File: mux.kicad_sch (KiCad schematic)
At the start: 6 parts, among them U24002 4066, U24003 4066, U24004 4075

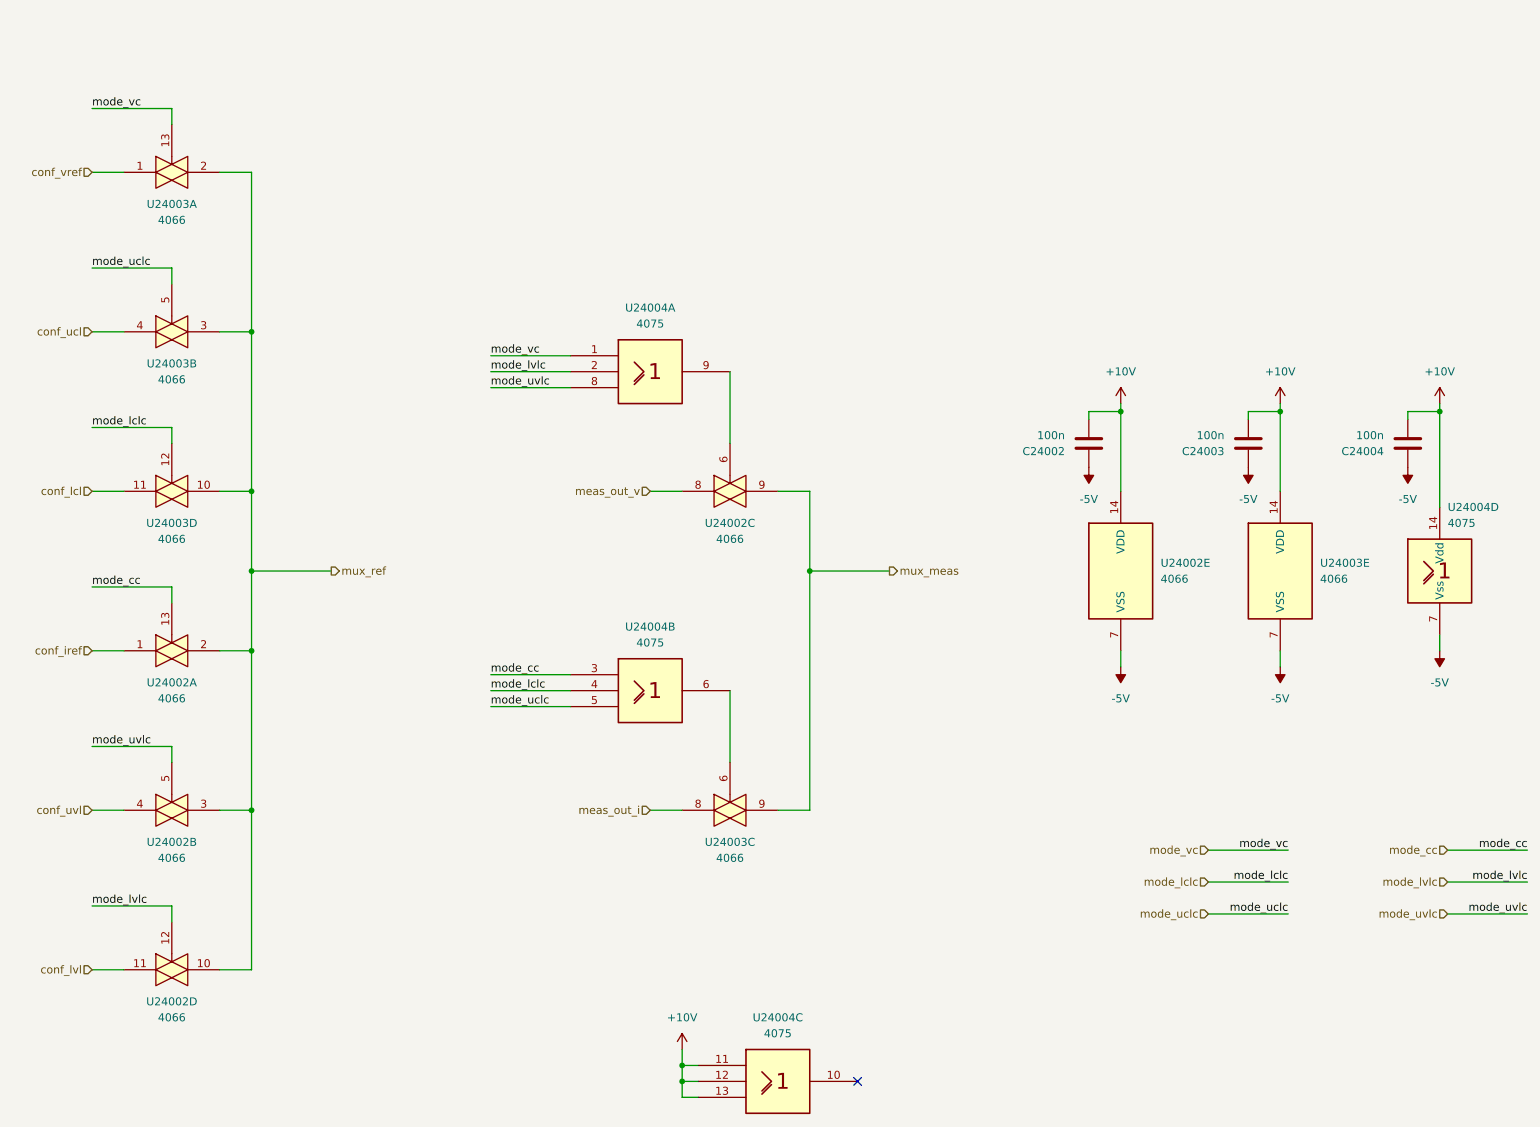
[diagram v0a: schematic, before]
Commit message: edit pss individual power nets for sub circuits
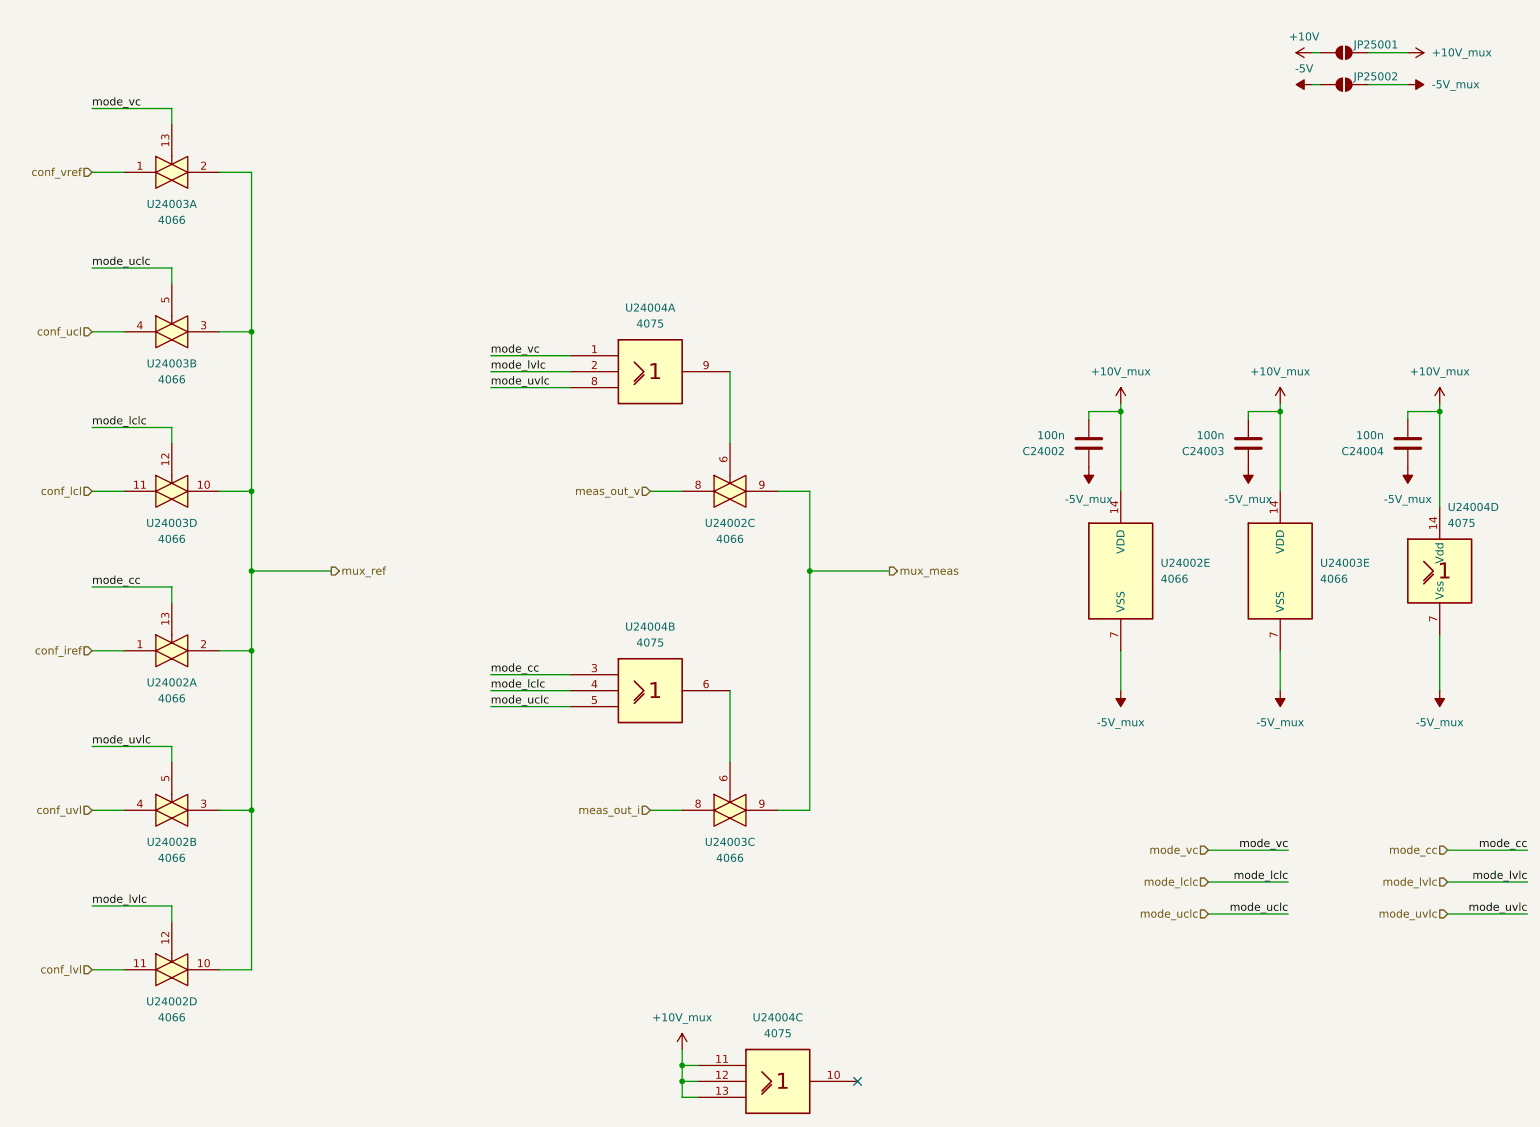
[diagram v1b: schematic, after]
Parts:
- added JP25001, JP25002: SolderJumper_2_Open, symbol Jumper:SolderJumper_2_Open
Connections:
- net +10V: now also JP25001.1 (A); no longer C24002.2, C24003.2, C24004.2, U24002.14 (VDD), U24003.14 (VDD), U24004.11, U24004.12, U24004.13, U24004.14 (Vdd)
- net -5V: now also JP25002.1 (A); no longer C24002.1, C24003.1, C24004.1, U24002.7 (VSS), U24003.7 (VSS), U24004.7 (Vss)
- new net +10V_mux: C24002.2, C24003.2, C24004.2, JP25001.2 (B), U24002.14 (VDD), U24003.14 (VDD), U24004.11, U24004.12, U24004.13, U24004.14 (Vdd)
- new net -5V_mux: C24002.1, C24003.1, C24004.1, JP25002.2 (B), U24002.7 (VSS), U24003.7 (VSS), U24004.7 (Vss)

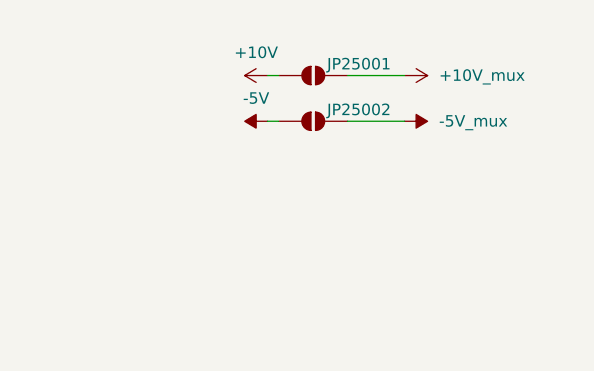
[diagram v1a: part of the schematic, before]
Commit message: fix pss ERC error: missing power flag
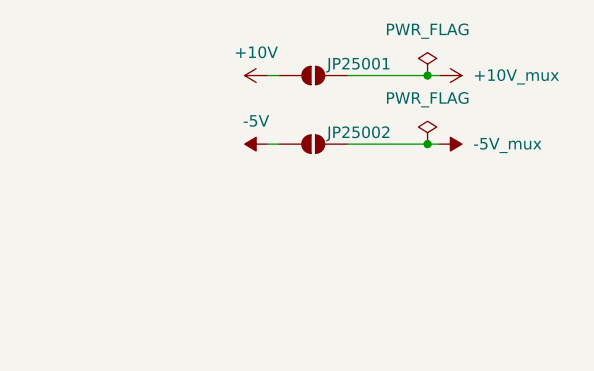
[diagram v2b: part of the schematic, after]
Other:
- moved on the sheet: JP25002
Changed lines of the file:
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@@
 	)
 	(junction
+		(at 262.89 25.4)
+		(diameter 0)
+		(color 0 0 0 0)
+	)
+	(junction
 		(at 240.03 82.55)
 		(diameter 0)
@@
 	)
 	(junction
+		(at 262.89 33.02)
+		(diameter 0)
+		(color 0 0 0 0)
+	)
+	(junction
 		(at 144.78 186.69)
 		(diameter 0)
@@
 	(wire
 		(pts
+			(xy 262.89 33.02) (xy 264.16 33.02)
+		)
+		(stroke
+			(width 0)
+			(type default)
+		)
+	)
+	(wire
+		(pts
 			(xy 234.95 83.82) (xy 234.95 82.55)
 		)
@@
 	(wire
 		(pts
-			(xy 245.11 30.48) (xy 246.38 30.48)
+			(xy 245.11 33.02) (xy 246.38 33.02)
 		)
 		(stroke
@@
 	(wire
 		(pts
-			(xy 254 30.48) (xy 260.35 30.48)
+			(xy 254 33.02) (xy 262.89 33.02)
 		)
 		(stroke
@@
 	(wire
 		(pts
-			(xy 254 25.4) (xy 260.35 25.4)
+			(xy 254 25.4) (xy 262.89 25.4)
 		)
 		(stroke
@@
 	(wire
 		(pts
+			(xy 262.89 25.4) (xy 264.16 25.4)
+		)
+		(stroke
+			(width 0)
+			(type default)
+		)
+	)
+	(wire
+		(pts
 			(xy 240.03 81.28) (xy 240.03 82.55)
 		)
@@
 	)
 	(symbol
+		(lib_id "pss:PWR_FLAG")
+		(at 262.89 33.02 0)
+		(unit 1)
+		(exclude_from_sim no)
+		(in_bom yes)
+		(on_board yes)
+		(dnp no)
+		(fields_autoplaced yes)
+		(property "Reference" "#FLG025002"
+			(at 262.89 31.115 0)
+			(effects
+				(font
+					(size 1.27 1.27)
+				)
+				(hide yes)
+			)
+		)
+		(property "Value" "PWR_FLAG"
+			(at 262.89 27.94 0)
+			(effects
+				(font
+					(size 1.27 1.27)
+				)
+			)
+		)
+		(property "Footprint" ""
+			(at 262.89 33.02 0)
+			(effects
+				(font
+					(size 1.27 1.27)
+				)
+				(hide yes)
+			)
+		)
+		(property "Datasheet" "~"
+			(at 262.89 33.02 0)
+			(effects
+				(font
+					(size 1.27 1.27)
+				)
+				(hide yes)
+			)
+		)
+		(property "Description" "Special symbol for telling ERC where power comes from"
+			(at 262.89 33.02 0)
+			(effects
+				(font
+					(size 1.27 1.27)
+				)
+				(hide yes)
+			)
+		)
+		(pin "1"
+		)
+		(instances
+			(project "pss"
+				(path "/3c438cf7-9350-4e9f-8115-1deba8984176/edd130f8-6d8c-4786-9c45-2e5306ef5419"
+					(reference "#FLG025002")
+					(unit 1)
+				)
+			)
+		)
+	)
+	(symbol
+		(lib_id "pss:PWR_FLAG")
+		(at 262.89 25.4 0)
+		(unit 1)
+		(exclude_from_sim no)
+		(in_bom yes)
+		(on_board yes)
+		(dnp no)
+		(fields_autoplaced yes)
+		(property "Reference" "#FLG025001"
+			(at 262.89 23.495 0)
+			(effects
+				(font
+					(size 1.27 1.27)
+				)
+				(hide yes)
+			)
+		)
+		(property "Value" "PWR_FLAG"
+			(at 262.89 20.32 0)
+			(effects
+				(font
+					(size 1.27 1.27)
+				)
+			)
+		)
+		(property "Footprint" ""
+			(at 262.89 25.4 0)
+			(effects
+				(font
+					(size 1.27 1.27)
+				)
+				(hide yes)
+			)
+		)
+		(property "Datasheet" "~"
+			(at 262.89 25.4 0)
+			(effects
+				(font
+					(size 1.27 1.27)
+				)
+				(hide yes)
+			)
+		)
+		(property "Description" "Special symbol for telling ERC where power comes from"
+			(at 262.89 25.4 0)
+			(effects
+				(font
+					(size 1.27 1.27)
+				)
+				(hide yes)
+			)
+		)
+		(pin "1"
+		)
+		(instances
+			(project "pss"
+				(path "/3c438cf7-9350-4e9f-8115-1deba8984176/edd130f8-6d8c-4786-9c45-2e5306ef5419"
+					(reference "#FLG025001")
+					(unit 1)
+				)
+			)
+		)
+	)
+	(symbol
 		(lib_id "pss:4075")
 		(at 160.02 189.23 0)
@@
 	(symbol
 		(lib_id "Jumper:SolderJumper_2_Open")
-		(at 250.19 30.48 0)
+		(at 250.19 33.02 0)
 		(unit 1)
 		(exclude_from_sim yes)
@@
 		(dnp no)
 		(property "Reference" "JP25002"
-			(at 255.27 29.21 0)
+			(at 255.27 31.75 0)
 			(effects
 				(font
@@
 		)
 		(property "Value" "SolderJumper_2_Open"
-			(at 224.79 17.78 0)
+			(at 224.79 20.32 0)
 			(effects
 				(font
@@
 		)
 		(property "Footprint" ""
-			(at 250.19 30.48 0)
+			(at 250.19 33.02 0)
 			(effects
 				(font
@@
 		)
 		(property "Datasheet" "~"
-			(at 250.19 30.48 0)
+			(at 250.19 33.02 0)
 			(effects
 				(font
@@
 		)
 		(property "Description" "Solder Jumper, 2-pole, open"
-			(at 250.19 30.48 0)
+			(at 250.19 33.02 0)
 			(effects
 				(font
@@
 	(symbol
 		(lib_id "pss:-5V_mux")
-		(at 260.35 30.48 270)
+		(at 264.16 33.02 270)
 		(unit 1)
 		(exclude_from_sim no)
@@
 		(fields_autoplaced yes)
 		(property "Reference" "#PWR025012"
-			(at 256.54 30.48 0)
+			(at 260.35 33.02 0)
 			(effects
 				(font
@@
 		)
 		(property "Value" "-5V_mux"
-			(at 264.16 30.4799 90)
+			(at 267.97 33.0199 90)
 			(effects
 				(font
@@
 		)
 		(property "Footprint" ""
-			(at 260.35 30.48 0)
+			(at 264.16 33.02 0)
 			(effects
 				(font
@@
 		)
 		(property "Datasheet" ""
-			(at 260.35 30.48 0)
+			(at 264.16 33.02 0)
 			(effects
 				(font
@@
 		)
 		(property "Description" ""
-			(at 260.35 30.48 0)
+			(at 264.16 33.02 0)
 			(effects
 				(font
@@
 	(symbol
 		(lib_id "pss:+10V_mux")
-		(at 260.35 25.4 270)
+		(at 264.16 25.4 270)
 		(unit 1)
 		(exclude_from_sim no)
@@
 		(fields_autoplaced yes)
 		(property "Reference" "#PWR025011"
-			(at 256.54 25.4 0)
+			(at 260.35 25.4 0)
 			(effects
 				(font
@@
 		)
 		(property "Value" "+10V_mux"
-			(at 264.16 25.3999 90)
+			(at 267.97 25.3999 90)
 			(effects
 				(font
@@
 		)
 		(property "Footprint" ""
-			(at 260.35 25.4 0)
+			(at 264.16 25.4 0)
 			(effects
 				(font
@@
 		)
 		(property "Datasheet" ""
-			(at 260.35 25.4 0)
+			(at 264.16 25.4 0)
 			(effects
 				(font
@@
 		)
 		(property "Description" ""
-			(at 260.35 25.4 0)
+			(at 264.16 25.4 0)
 			(effects
 				(font
@@
 	(symbol
 		(lib_id "pss:-5V")
-		(at 245.11 30.48 90)
+		(at 245.11 33.02 90)
 		(unit 1)
 		(exclude_from_sim no)
@@
 		(fields_autoplaced yes)
 		(property "Reference" "#PWR025006"
-			(at 248.92 30.48 0)
+			(at 248.92 33.02 0)
 			(effects
 				(font
@@
 		)
 		(property "Value" "-5V"
-			(at 243.84 27.94 90)
+			(at 243.84 30.48 90)
 			(effects
 				(font
@@
 		)
 		(property "Footprint" ""
-			(at 245.11 30.48 0)
+			(at 245.11 33.02 0)
 			(effects
 				(font
@@
 		)
 		(property "Datasheet" ""
-			(at 245.11 30.48 0)
+			(at 245.11 33.02 0)
 			(effects
 				(font
@@
 		)
 		(property "Description" "Power symbol creates a global label with name \"-5V\""
-			(at 245.11 30.48 0)
+			(at 245.11 33.02 0)
 			(effects
 				(font

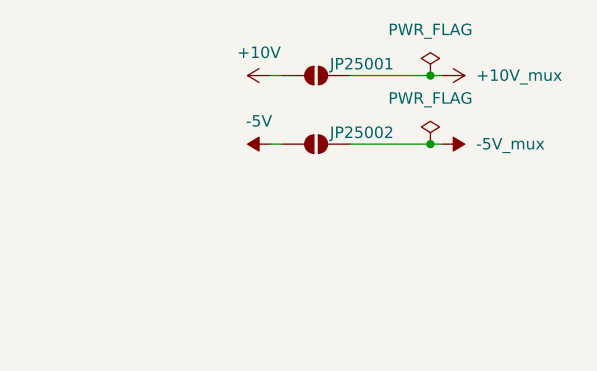
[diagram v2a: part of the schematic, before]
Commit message: fix pss ERC errors: multiple outputs connected
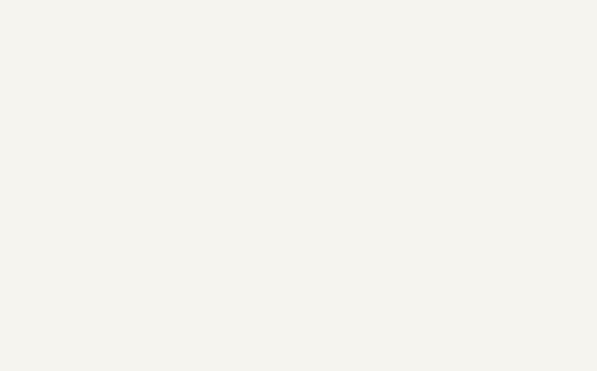
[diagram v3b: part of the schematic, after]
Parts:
- removed JP25001, JP25002: SolderJumper_2_Open, symbol Jumper:SolderJumper_2_Open
